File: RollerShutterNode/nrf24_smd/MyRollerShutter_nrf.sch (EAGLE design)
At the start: 50 parts, among them IC1 ATMega-328, IC2 AT25DF512C-SSHN-B, IC3 MCP1703CB, IC4 ACS712_5A, IC5 ATSHA204A, IC6 LM321, IC7 MDC3105DMT1, X1 8 MHz

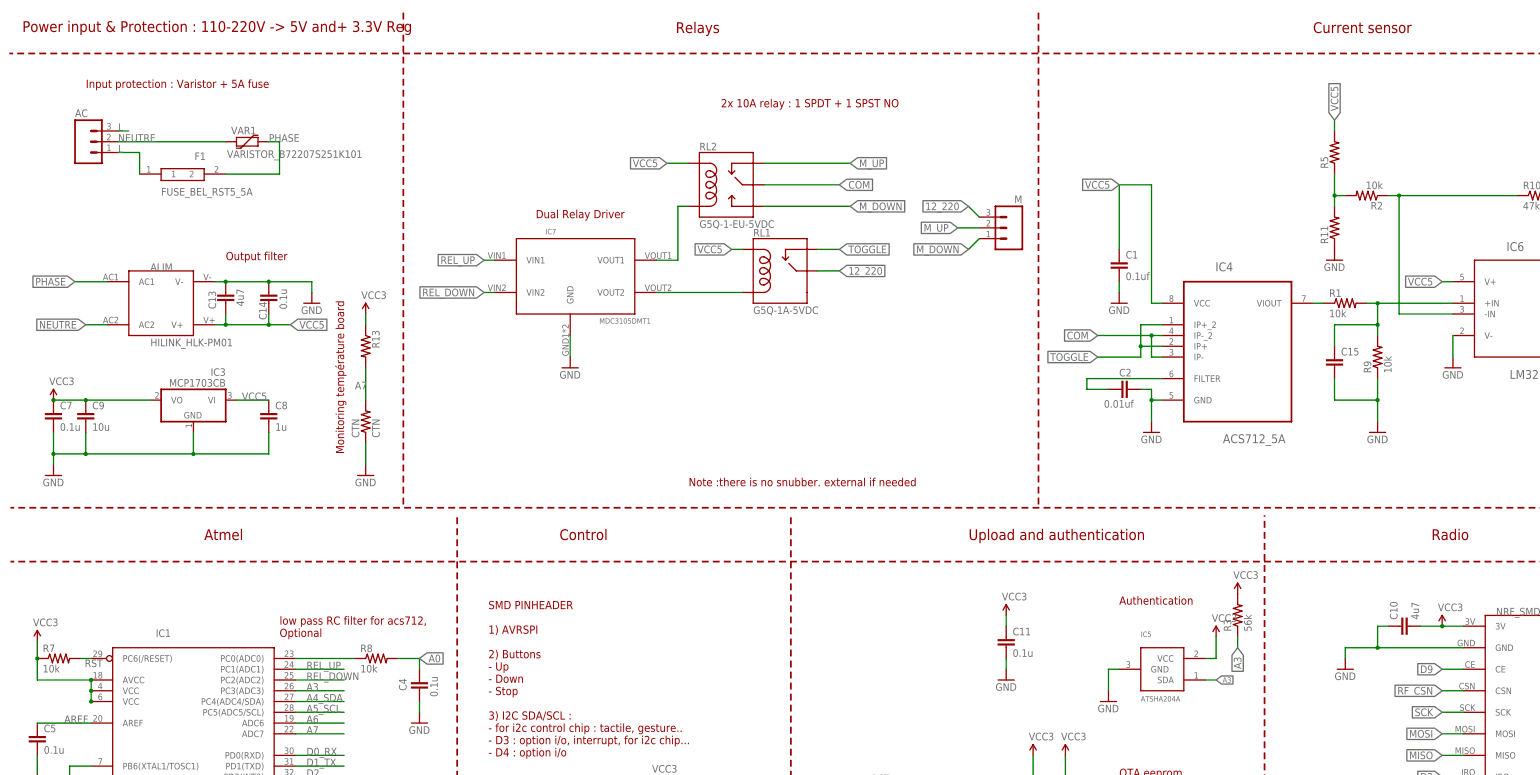
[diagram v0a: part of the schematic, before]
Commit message: some rerouting and a small fix on connector
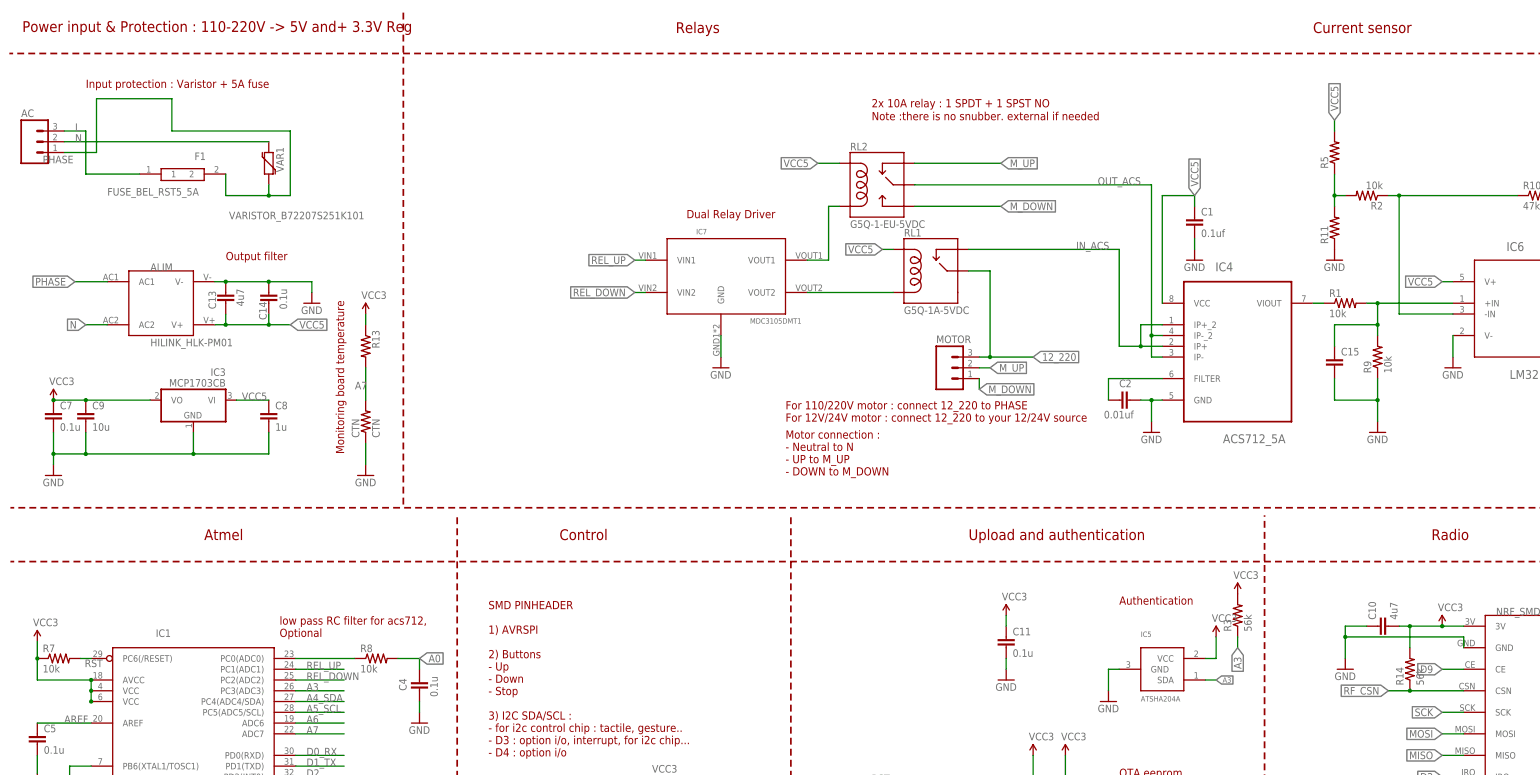
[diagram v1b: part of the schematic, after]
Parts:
- removed M: (no value), SparkFun-Connectors:M03-SCREW-5MM
- added MOTOR: (no value), SparkFun-Connectors:M03-SCREW-5MM
- added R14: 56k, LowPowerLab:RESISTOR0805-RES
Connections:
- net COM renamed OUT_ACS
- net NEUTRE renamed N
- net TOGGLE renamed IN_ACS
- net 12_220: now also MOTOR.3; no longer M.3
- net L: no longer AC.1
- net M_DOWN: now also MOTOR.1; no longer M.1
- net M_UP: now also MOTOR.2; no longer M.2
- net PHASE: now also AC.1
- net RF_CSN: now also R14.1
- net VCC: now also R14.2
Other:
- note added: "For 110/220V motor : connect 12_220 to PHASE For 12V/24V motor : connect 12_220 to your 12/24V source"
- note added: "Monitoring board temperature"
- note added: "Motor connection : - Neutral to N - UP to M_UP - DOWN to M_DOWN"
- note removed: "Monitoring température board"
- moved on the sheet: AC, C1, C10, C2, IC7, RL1, RL2, VAR1
